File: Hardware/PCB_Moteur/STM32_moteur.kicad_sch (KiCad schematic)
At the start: 59 parts, among them J2 Conn_01x06_Pin, U2 STM32F103CBT6

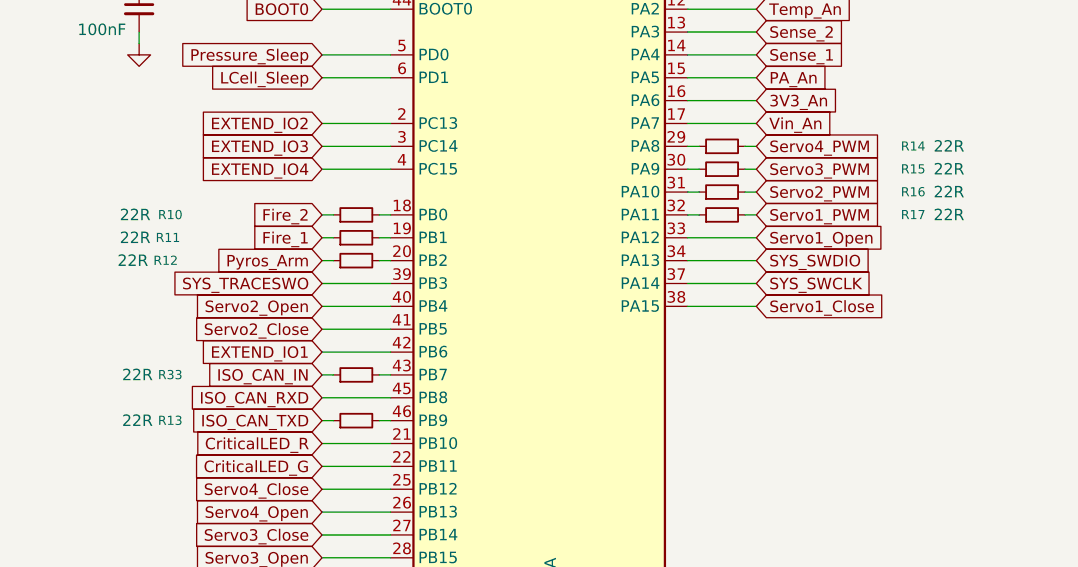
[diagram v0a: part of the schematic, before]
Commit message: wip: fin layout CAN et interface servo
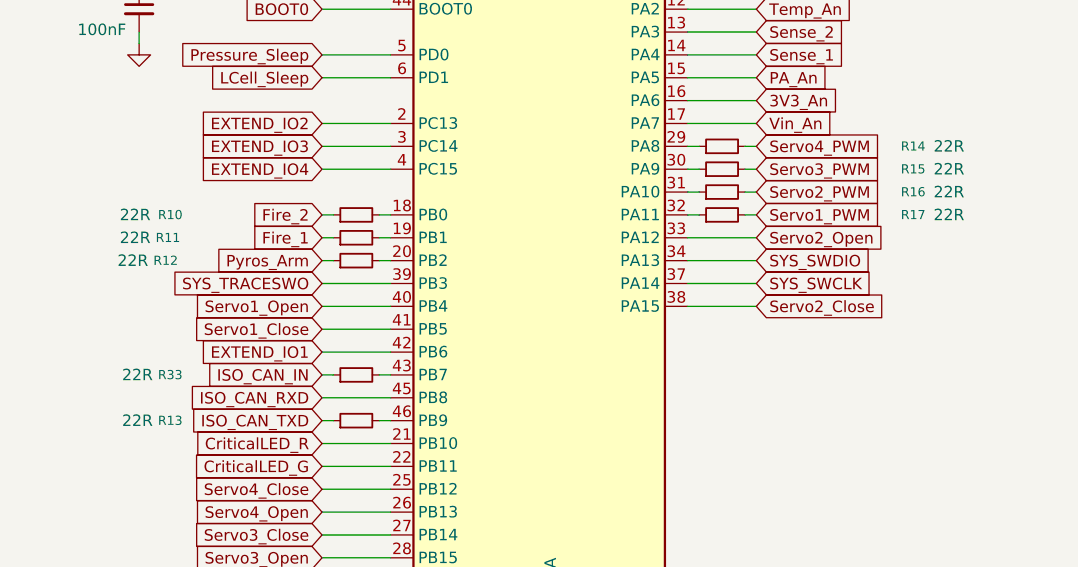
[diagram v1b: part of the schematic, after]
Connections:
- net Servo1_Close: now also U2.41 (PB5); no longer U2.38 (PA15)
- net Servo1_Open: now also U2.40 (PB4); no longer U2.33 (PA12)
- net Servo2_Close: now also U2.38 (PA15); no longer U2.41 (PB5)
- net Servo2_Open: now also U2.33 (PA12); no longer U2.40 (PB4)

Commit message: wip: layout presque fini (decoup stm32 restant)
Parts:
- C21, C22: footprint Capacitor_SMD:C_0805_2012Metric -> Capacitor_SMD:C_0603_1608Metric
- R10, R11, R12, R13, R14, R15, R16, R17, R33, R8, R9: footprint Resistor_SMD:R_0805_2012Metric -> Resistor_SMD:R_0603_1608Metric
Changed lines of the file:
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@@
 			)
 		)
-		(property "Footprint" "Resistor_SMD:R_0805_2012Metric"
+		(property "Footprint" "Resistor_SMD:R_0603_1608Metric"
 			(at 170.18 74.93 0)
 			(effects
@@
 			)
 		)
-		(property "Footprint" "Capacitor_SMD:C_0805_2012Metric"
+		(property "Footprint" "Capacitor_SMD:C_0603_1608Metric"
 			(at 250.4948 80.01 0)
 			(effects
@@
 			)
 		)
-		(property "Footprint" "Resistor_SMD:R_0805_2012Metric"
+		(property "Footprint" "Resistor_SMD:R_0603_1608Metric"
 			(at 129.54 80.01 0)
 			(effects
@@
 			)
 		)
-		(property "Footprint" "Resistor_SMD:R_0805_2012Metric"
+		(property "Footprint" "Resistor_SMD:R_0603_1608Metric"
 			(at 129.54 97.79 0)
 			(effects
@@
 			)
 		)
-		(property "Footprint" "Resistor_SMD:R_0805_2012Metric"
+		(property "Footprint" "Resistor_SMD:R_0603_1608Metric"
 			(at 261.62 23.622 90)
 			(effects
@@
 			)
 		)
-		(property "Footprint" "Capacitor_SMD:C_0805_2012Metric"
+		(property "Footprint" "Capacitor_SMD:C_0603_1608Metric"
 			(at 264.4648 80.01 0)
 			(effects
@@
 			)
 		)
-		(property "Footprint" "Resistor_SMD:R_0805_2012Metric"
+		(property "Footprint" "Resistor_SMD:R_0603_1608Metric"
 			(at 170.18 72.39 0)
 			(effects
@@
 			)
 		)
-		(property "Footprint" "Resistor_SMD:R_0805_2012Metric"
+		(property "Footprint" "Resistor_SMD:R_0603_1608Metric"
 			(at 170.18 77.47 0)
 			(effects
@@
 			)
 		)
-		(property "Footprint" "Resistor_SMD:R_0805_2012Metric"
+		(property "Footprint" "Resistor_SMD:R_0603_1608Metric"
 			(at 129.54 85.09 0)
 			(effects
@@
 			)
 		)
-		(property "Footprint" "Resistor_SMD:R_0805_2012Metric"
+		(property "Footprint" "Resistor_SMD:R_0603_1608Metric"
 			(at 170.18 80.01 0)
 			(effects
@@
 			)
 		)
-		(property "Footprint" "Resistor_SMD:R_0805_2012Metric"
+		(property "Footprint" "Resistor_SMD:R_0603_1608Metric"
 			(at 129.54 82.55 0)
 			(effects
@@
 			)
 		)
-		(property "Footprint" "Resistor_SMD:R_0805_2012Metric"
+		(property "Footprint" "Resistor_SMD:R_0603_1608Metric"
 			(at 129.54 102.87 0)
 			(effects
@@
 			)
 		)
-		(property "Footprint" "Resistor_SMD:R_0805_2012Metric"
+		(property "Footprint" "Resistor_SMD:R_0603_1608Metric"
 			(at 269.748 30.48 90)
 			(effects

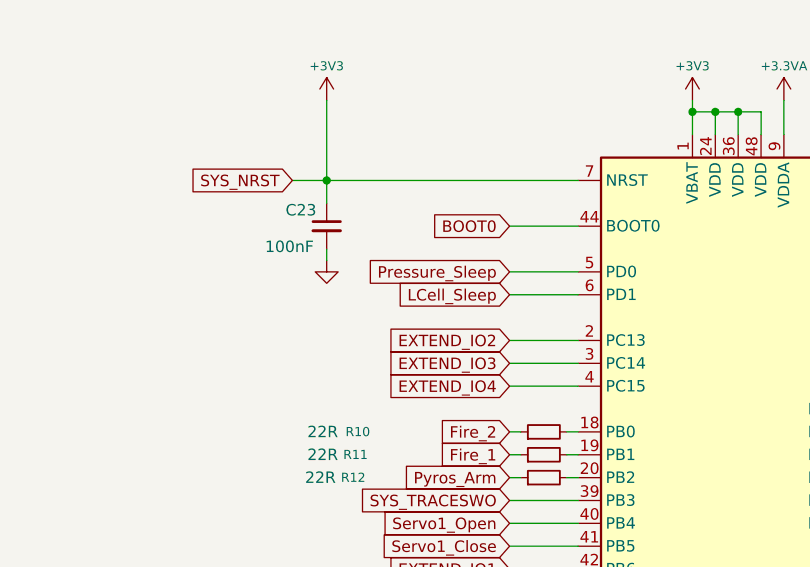
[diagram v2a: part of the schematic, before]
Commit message: feat: copy all existing schematics in gse project + add missing components + fix voltage divider for 3S + create gse project and seperate stm32 project + add missing resistors motor
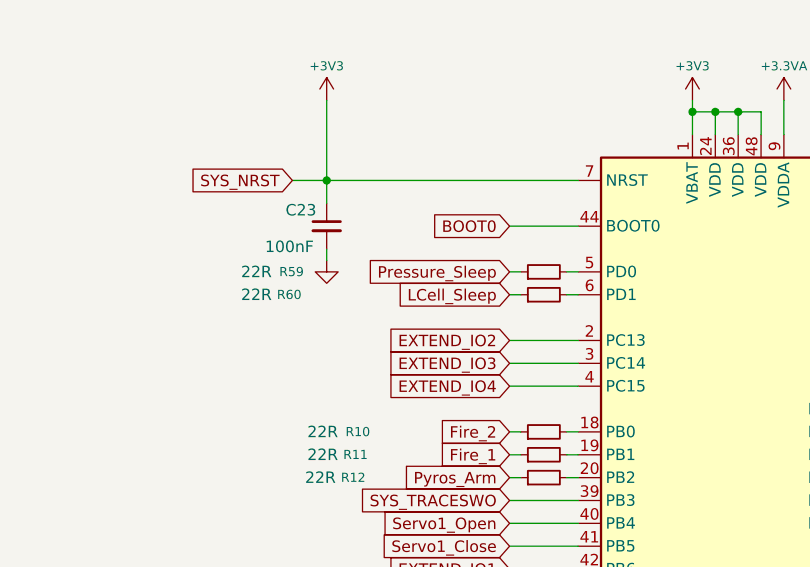
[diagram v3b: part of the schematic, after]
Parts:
- added R59, R60: 22R, Resistor_SMD:R_0603_1608Metric, symbol Device:R_Small
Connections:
- net LCell_Sleep: now also R60.1; no longer U2.6 (PD1)
- net Pressure_Sleep: now also R59.1; no longer U2.5 (PD0)
- new net: R59.2, U2.5 (PD0)
- new net: R60.2, U2.6 (PD1)
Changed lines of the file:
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@@
 	(wire
 		(pts
-			(xy 125.73 62.23) (xy 133.35 62.23)
-		)
-		(stroke
-			(width 0)
-			(type default)
-		)
-	)
-	(wire
-		(pts
 			(xy 166.37 87.63) (xy 173.99 87.63)
 		)
@@
 	(wire
 		(pts
-			(xy 125.73 64.77) (xy 133.35 64.77)
+			(xy 125.73 62.23) (xy 127 62.23)
 		)
 		(stroke
@@
 	(wire
 		(pts
+			(xy 125.73 64.77) (xy 127 64.77)
+		)
+		(stroke
+			(width 0)
+			(type default)
+		)
+	)
+	(wire
+		(pts
 			(xy 105.41 43.18) (xy 105.41 52.07)
 		)
@@
 	(wire
 		(pts
+			(xy 132.08 62.23) (xy 133.35 62.23)
+		)
+		(stroke
+			(width 0)
+			(type default)
+		)
+	)
+	(wire
+		(pts
+			(xy 132.08 64.77) (xy 133.35 64.77)
+		)
+		(stroke
+			(width 0)
+			(type default)
+		)
+	)
+	(wire
+		(pts
 			(xy 125.73 118.11) (xy 133.35 118.11)
 		)
@@
 	)
 	(symbol
+		(lib_id "Device:R_Small")
+		(at 129.54 64.77 90)
+		(unit 1)
+		(exclude_from_sim no)
+		(in_bom yes)
+		(on_board yes)
+		(dnp no)
+		(property "Reference" "R60"
+			(at 102.616 64.77 90)
+			(effects
+				(font
+					(size 1.016 1.016)
+				)
+				(justify left)
+			)
+		)
+		(property "Value" "22R"
+			(at 99.314 64.77 90)
+			(effects
+				(font
+					(size 1.27 1.27)
+				)
+				(justify left)
+			)
+		)
+		(property "Footprint" "Resistor_SMD:R_0603_1608Metric"
+			(at 129.54 64.77 0)
+			(effects
+				(font
+					(size 1.27 1.27)
+				)
+				(hide yes)
+			)
+		)
+		(property "Datasheet" "~"
+			(at 129.54 64.77 0)
+			(effects
+				(font
+					(size 1.27 1.27)
+				)
+				(hide yes)
+			)
+		)
+		(property "Description" "Resistor, small symbol"
+			(at 129.54 64.77 0)
+			(effects
+				(font
+					(size 1.27 1.27)
+				)
+				(hide yes)
+			)
+		)
+		(pin "1"
+		)
+		(pin "2"
+		)
+		(instances
+			(project "PCB_moteur"
+				(path "/b0d87684-7b1c-41d8-8358-755aa327573e/753d1783-c2f5-4012-bbb8-3f4eadf066f6"
+					(reference "R60")
+					(unit 1)
+				)
+			)
+		)
+	)
+	(symbol
 		(lib_id "Connector:TestPoint")
 		(at 238.76 160.02 270)
@@
 					(unit 1)
 				)
+			)
+		)
+	)
+	(symbol
+		(lib_id "Device:R_Small")
+		(at 129.54 62.23 90)
+		(unit 1)
+		(exclude_from_sim no)
+		(in_bom yes)
+		(on_board yes)
+		(dnp no)
+		(property "Reference" "R59"
+			(at 102.87 62.23 90)
+			(effects
+				(font
+					(size 1.016 1.016)
+				)
+				(justify left)
+			)
+		)
+		(property "Value" "22R"
+			(at 99.314 62.23 90)
+			(effects
+				(font
+					(size 1.27 1.27)
+				)
+				(justify left)
+			)
+		)
+		(property "Footprint" "Resistor_SMD:R_0603_1608Metric"
+			(at 129.54 62.23 0)
+			(effects
+				(font
+					(size 1.27 1.27)
+				)
+				(hide yes)
+			)
+		)
+		(property "Datasheet" "~"
+			(at 129.54 62.23 0)
+			(effects
+				(font
+					(size 1.27 1.27)
+				)
+				(hide yes)
+			)
+		)
+		(property "Description" "Resistor, small symbol"
+			(at 129.54 62.23 0)
+			(effects
+				(font
+					(size 1.27 1.27)
+				)
+				(hide yes)
+			)
+		)
+		(pin "1"
+		)
+		(pin "2"
+		)
+		(instances
+			(project "PCB_moteur"
+				(path "/b0d87684-7b1c-41d8-8358-755aa327573e/753d1783-c2f5-4012-bbb8-3f4eadf066f6"
+					(reference "R59")
+					(unit 1)
+				)

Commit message: wip: routing sys et limit switches
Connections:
- net SYS_TRACESWO is gone; now on net SYS_SWO: U2.39 (PB3)
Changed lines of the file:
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@@
 		)
 	)
-	(global_label "SYS_TRACESWO"
+	(global_label "SYS_SWO"
 		(shape input)
 		(at 125.73 87.63 180)
@@
 		)
 		(property "Intersheetrefs" "${INTERSHEET_REFS}"
-			(at 108.533 87.63 0)
+			(at 114.2782 87.63 0)
 			(effects
 				(font

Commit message: wip: routing, bientot plane d'alim!
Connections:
- net CriticalLED_G: now also U2.21 (PB10); no longer U2.22 (PB11)
- net CriticalLED_R: now also U2.22 (PB11); no longer U2.21 (PB10)
- net Fire_1: now also R10.1; no longer R11.1
- net Fire_2: now also R11.1; no longer R10.1
- net Sense_1: now also U2.13 (PA3); no longer U2.14 (PA4)
- net Sense_2: now also U2.14 (PA4); no longer U2.13 (PA3)

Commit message: wip: reste plane
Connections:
- net 3V3_An: now also U2.17 (PA7); no longer U2.16 (PA6)
- net Vin_An: now also U2.16 (PA6); no longer U2.17 (PA7)

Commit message: refactor: merge emile + main branches
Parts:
- added R61: 10k, Resistor_SMD:R_0805_2012Metric, symbol Device:R_Small
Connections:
- net +3V3: now also R61.2; no longer C23.1, J2.6 (Pin_6), U2.7 (NRST)
- new net SYS_NRST: C23.1, J2.6 (Pin_6), R61.1, U2.7 (NRST)

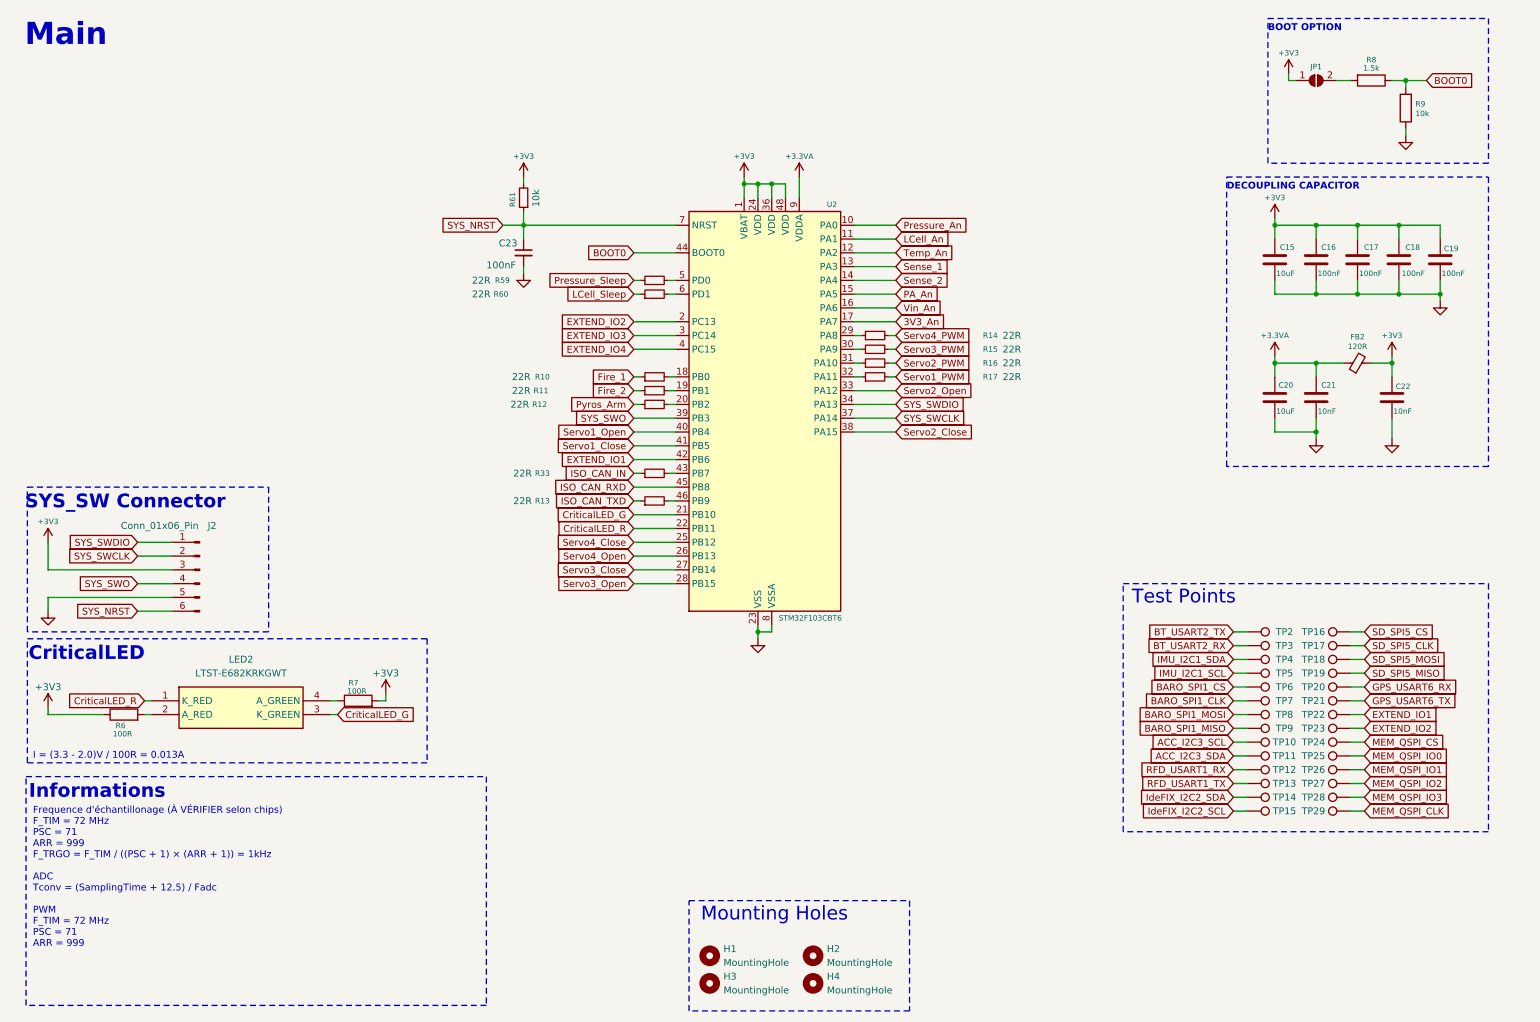
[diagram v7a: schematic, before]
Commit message: feat(moteur): add 8MHz crystal (only schematic), fix ERC, update stm32 project, remove extend ios
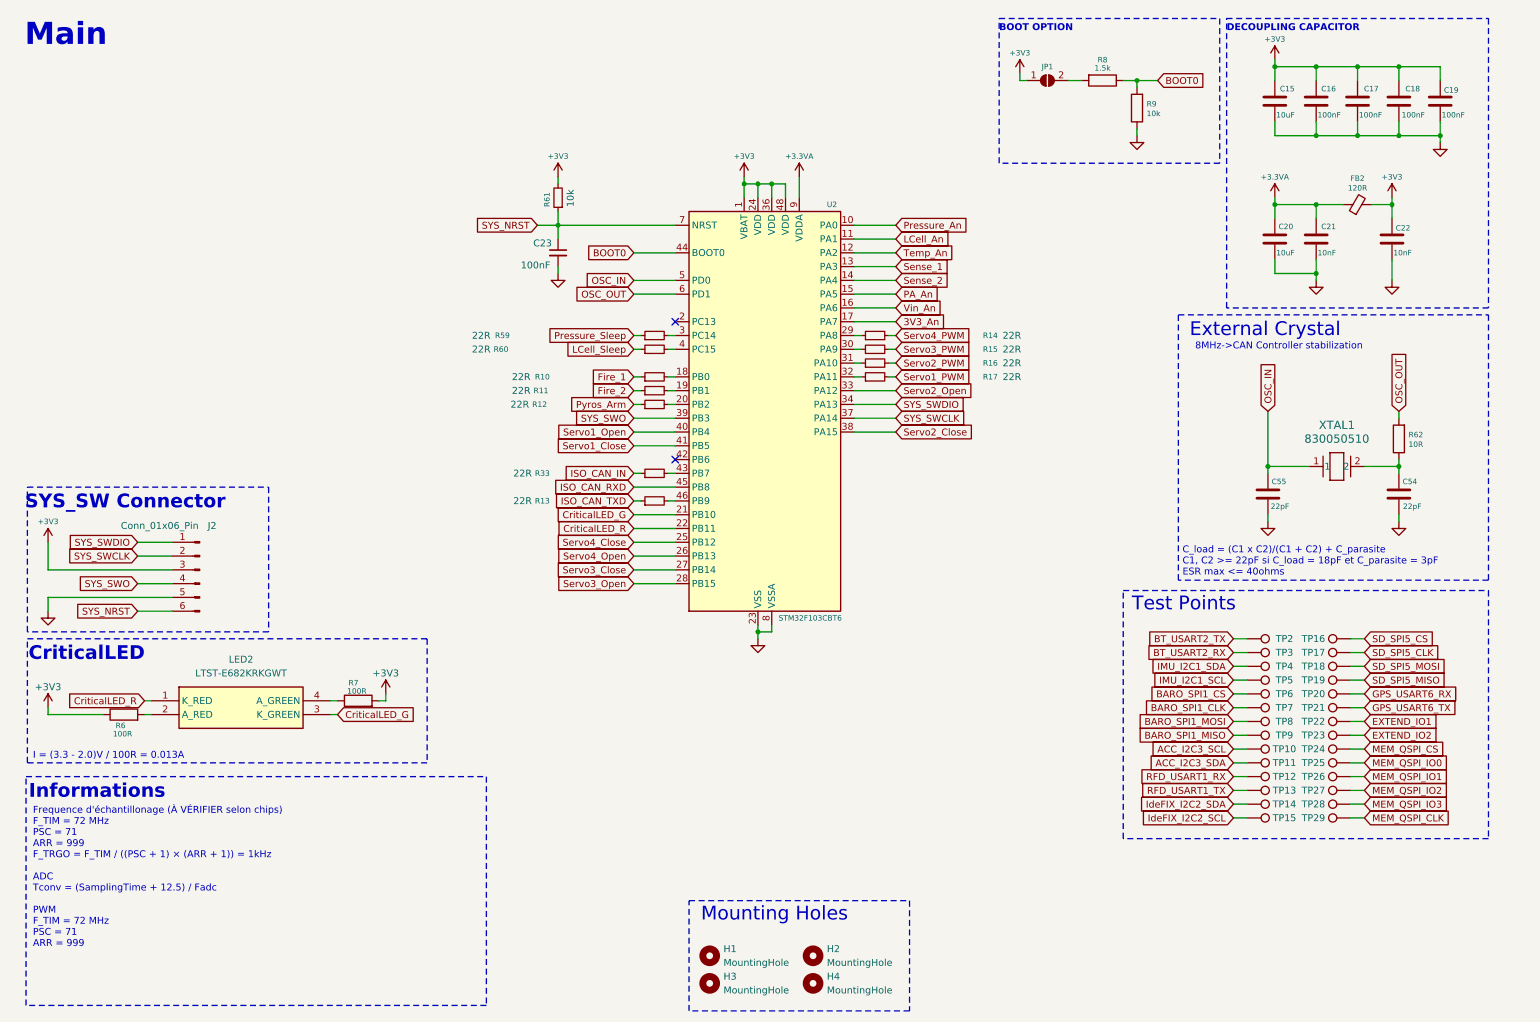
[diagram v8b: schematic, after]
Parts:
- added C54, C55: 22pF, Capacitor_SMD:C_0805_2012Metric, symbol Device:C
- added R62: 10R, Resistor_SMD:R_0805_2012Metric, symbol Device:R
- added XTAL1: 830050510, pcb_moteur:830050510, symbol pcb_moteur:830050510
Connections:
- net EXTEND_IO3 is gone; now on an unnamed net: U2.3 (PC14)
- net EXTEND_IO4 is gone; now on an unnamed net: U2.4 (PC15)
- net EXTEND_IO1: no longer U2.42 (PB6)
- net EXTEND_IO2: no longer U2.2 (PC13)
- net GND: now also C54.1, C55.1
- net at R59.2: no longer U2.5 (PD0)
- net at R60.2: no longer U2.6 (PD1)
- new net: C54.2, R62.1, XTAL1.2
- new net OSC_IN: C55.2, U2.5 (PD0), XTAL1.1
- new net OSC_OUT: R62.2, U2.6 (PD1)
- no-connect marks 0 -> 2
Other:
- note added: "8MHz->CAN Controller stabilization"
- note added: "C_load = (C1 x C2)/(C1 + C2) + C_parasite C1, C2 >= 22pF si C_load = 18pF et C_parasite = 3pF ESR max <= 40ohms"
- note added: "External Crystal"
- moved on the sheet: C15, C16, C17, C18, C19, C20, C21, C22, C23, FB2, JP1, R59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
